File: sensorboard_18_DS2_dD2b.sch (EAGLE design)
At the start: 89 parts, among them IC1 ECMF02-2AMX6, IC2_ESP32S2WROOMM22S2 ESP32-S2-WROOM_M22S2H3200PH3Q0, J1_CONN._ADAPTERB. RJ12, J4_USB USB_CONN, J6_OAT 2.5mm JACK, J7_I2C RJ12, U1 LPS22HB, U10-MAG_SENSOR MMC5983MA, U11 LDL212PV33R, U12 NCV8163ASN330T1G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

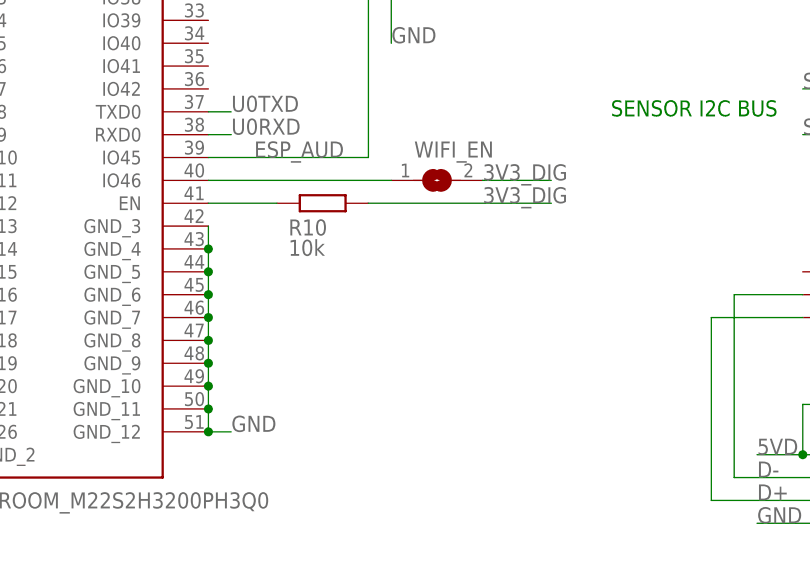
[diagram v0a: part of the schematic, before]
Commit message: Upload sensorboard_18_DS2_dD2b files
Add ESP32 EN pin bypass capacitor

Remove sensorboard_18_DS2_dD2 files
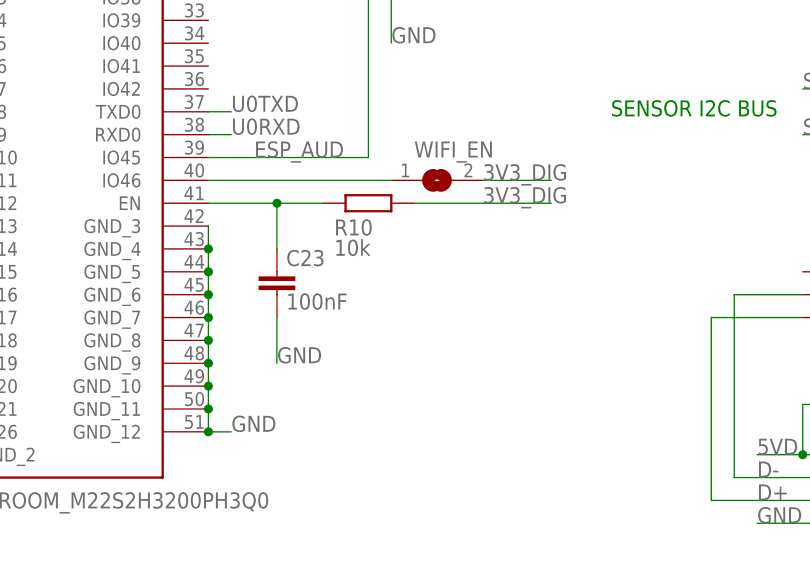
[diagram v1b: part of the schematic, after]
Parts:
- added C23: 100nF, rcl:C-EUC0805
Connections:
- net GND: now also C23.2
- net N$7: now also C23.1
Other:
- moved on the sheet: R10
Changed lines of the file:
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@@
 <part name="J6_OAT" library="SamacSys_Parts" deviceset="SJ-2523-SMT-TR" device="" value="2.5mm JACK"/>
 <part name="ESP_AUD" library="pinhead" library_urn="urn:adsk.eagle:library:325" deviceset="PINHD-1X2" device="" package3d_urn="urn:adsk.eagle:package:22435/2"/>
+<part name="C23" library="rcl" library_urn="urn:adsk.eagle:library:334" deviceset="C-EU" device="C0805" package3d_urn="urn:adsk.eagle:package:23617/2" value="100nF"/>
 </parts>
 <sheets>
@@
 <attribute name="VALUE" x="214.63" y="-77.47" size="1.778" layer="96" align="center-left"/>
 </instance>
-<instance part="R10" gate="G$1" x="162.56" y="73.66" smashed="yes">
-<attribute name="NAME" x="158.75" y="70.0786" size="1.778" layer="95"/>
-<attribute name="VALUE" x="158.75" y="67.818" size="1.778" layer="96"/>
+<instance part="R10" gate="G$1" x="167.64" y="73.66" smashed="yes">
+<attribute name="NAME" x="163.83" y="70.0786" size="1.778" layer="95"/>
+<attribute name="VALUE" x="163.83" y="67.818" size="1.778" layer="96"/>
 </instance>
 <instance part="12V_IN" gate="-1" x="5.08" y="-81.28" smashed="yes" rot="R180">
@@
 <attribute name="NAME" x="173.99" y="104.775" size="1.778" layer="95"/>
 <attribute name="VALUE" x="173.99" y="93.98" size="1.778" layer="96"/>
+</instance>
+<instance part="C23" gate="G$1" x="157.48" y="66.04" smashed="yes">
+<attribute name="NAME" x="158.496" y="66.675" size="1.778" layer="95"/>
+<attribute name="VALUE" x="158.496" y="61.849" size="1.778" layer="96"/>
 </instance>
 </instances>
@@
 <label x="170.18" y="91.44" size="1.778" layer="95"/>
 </segment>
+<segment>
+<pinref part="C23" gate="G$1" pin="2"/>
+<wire x1="157.48" y1="60.96" x2="157.48" y2="55.88" width="0.1524" layer="91"/>
+<label x="157.48" y="55.88" size="1.778" layer="95"/>
+</segment>
 </net>
 <net name="VDD1" class="0">
@@
 <pinref part="R10" gate="G$1" pin="1"/>
 <pinref part="IC2_ESP32S2WROOMM22S2" gate="G$1" pin="EN"/>
+<wire x1="162.56" y1="73.66" x2="157.48" y2="73.66" width="0.1524" layer="91"/>
+<pinref part="C23" gate="G$1" pin="1"/>
 <wire x1="157.48" y1="73.66" x2="149.86" y2="73.66" width="0.1524" layer="91"/>
+<wire x1="157.48" y1="68.58" x2="157.48" y2="73.66" width="0.1524" layer="91"/>
+<junction x="157.48" y="73.66"/>
 </segment>
 </net>
@@
 <segment>
 <pinref part="R10" gate="G$1" pin="2"/>
-<wire x1="167.64" y1="73.66" x2="187.96" y2="73.66" width="0.1524" layer="91"/>
+<wire x1="172.72" y1="73.66" x2="187.96" y2="73.66" width="0.1524" layer="91"/>
 <label x="180.34" y="73.66" size="1.778" layer="95"/>
 </segment>
